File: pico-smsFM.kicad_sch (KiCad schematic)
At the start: 30 parts, among them J1 AudioJack3_SwitchTR, U1 Pico, U2 YM2413, U3 SN76489, U4 AE-Si5351A, U5 NJM4580, U6 4066

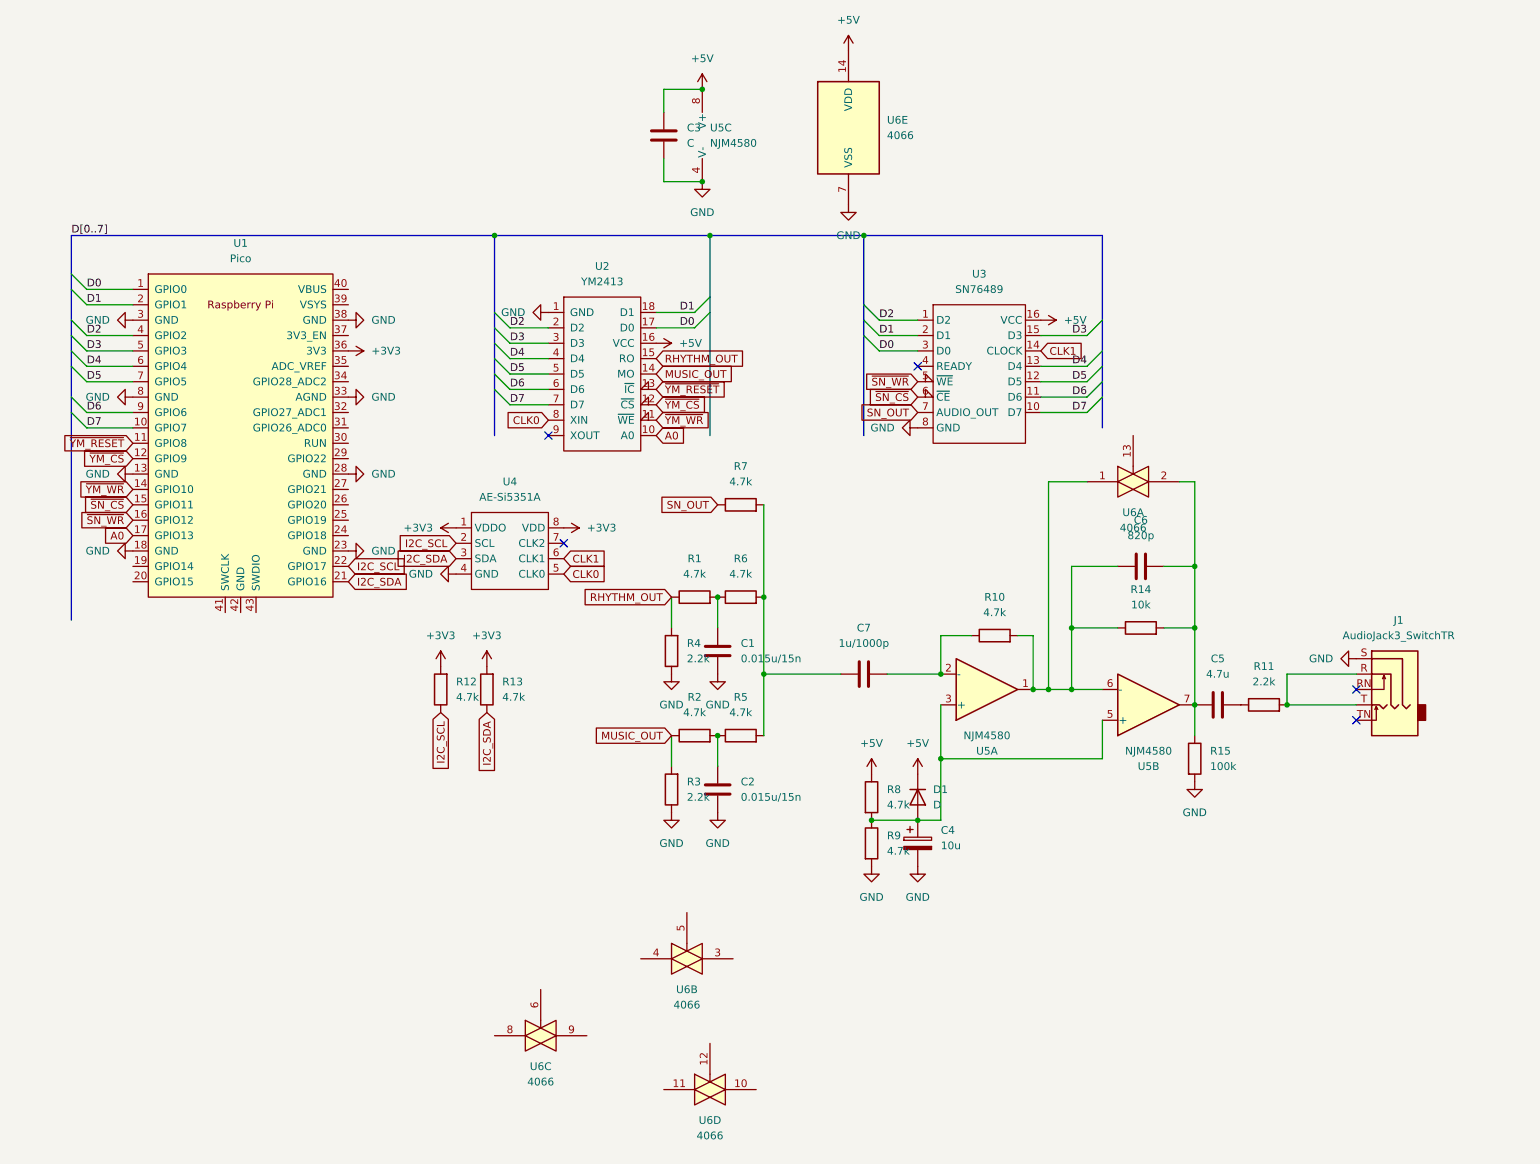
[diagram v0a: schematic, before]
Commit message: Add decoupling cap
Add more logic wire
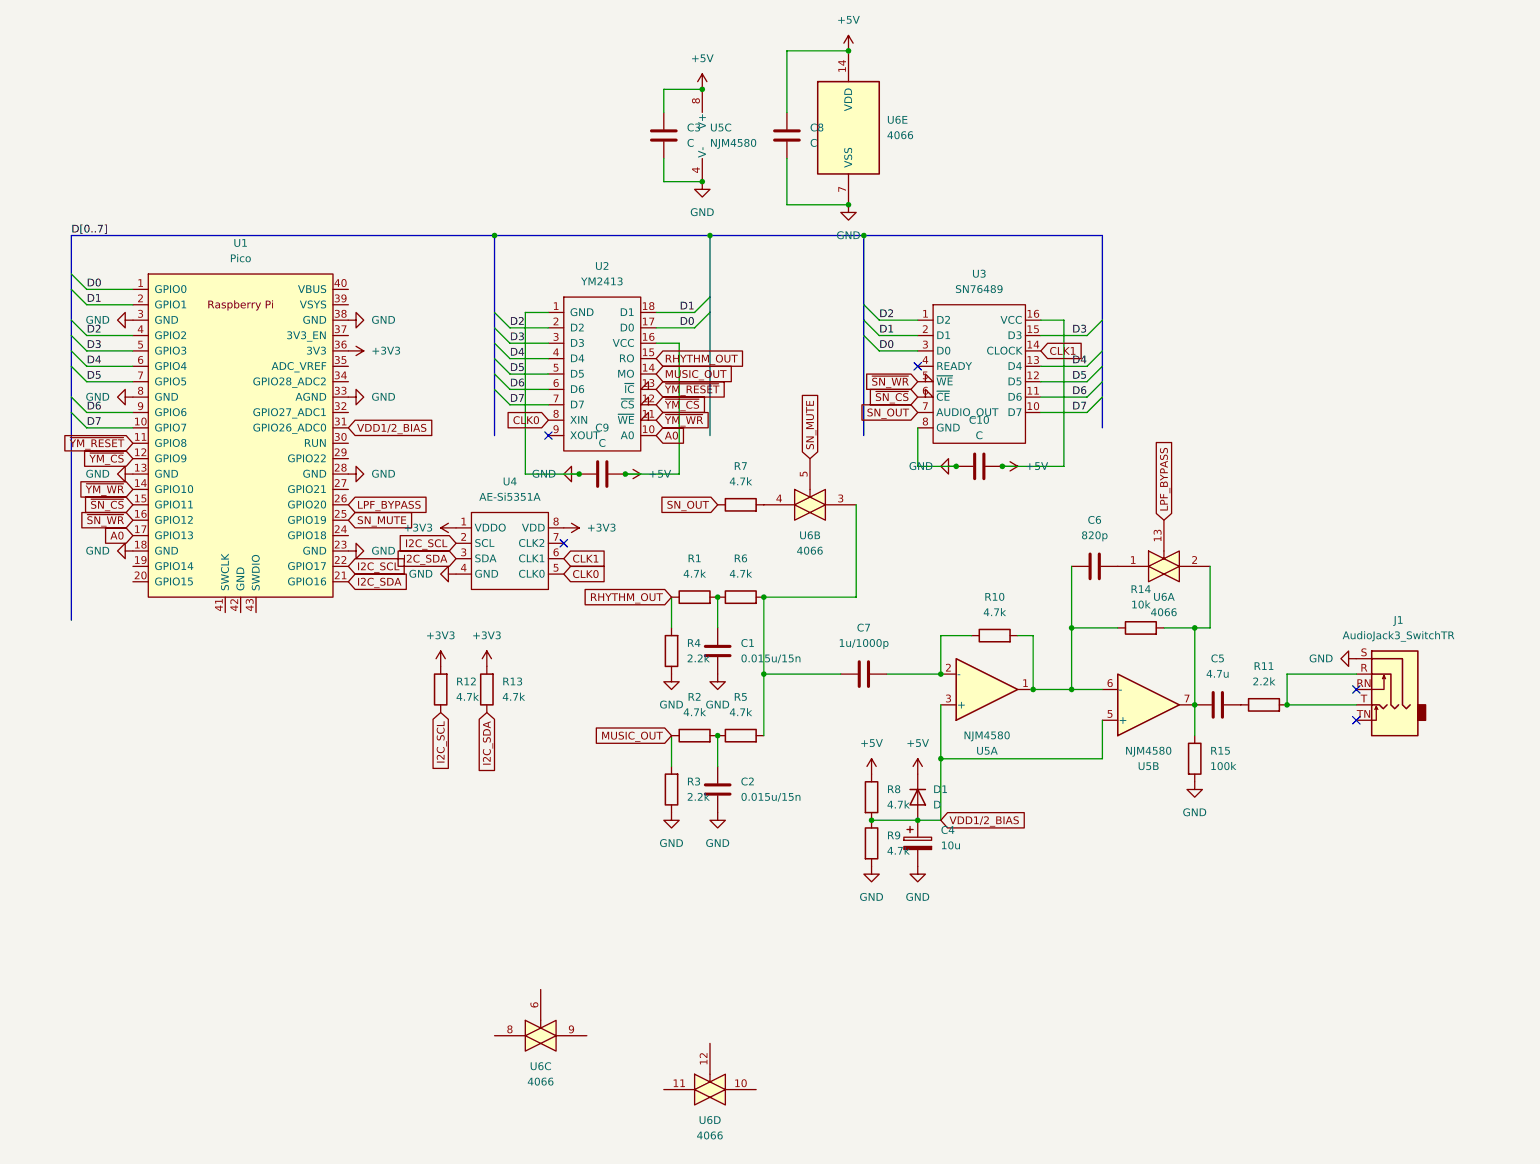
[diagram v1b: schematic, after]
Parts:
- added C10, C8, C9: C, Capacitor_THT:CP_Radial_D6.3mm_P2.50mm, symbol Device:C
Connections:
- net +5V: now also C10.2, C8.1, C9.2
- net GND: now also C10.1, C8.2, C9.1
- net VDD1/2_BIAS: now reaches C4.1, D1.2 (A), R8.2, R9.1, U5.3 (+), U5.5 (+)
- net VDD1/2_BIAS: now also U1.31 (GPIO26_ADC0)
- net at C7.1, R5.2, R6.2: now also U6.3; no longer R7.2
- net at C6.1, R10.2, R14.1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: no longer U6.1
- net at C5.1, R14.2, R15.1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: no longer C6.2
- net SN_MUTE: now reaches U1.25 (GPIO19)
- net SN_MUTE: now also U6.5
- net LPF_BYPASS: now reaches U1.26 (GPIO20)
- net LPF_BYPASS: now also U6.13
- net at U6.4: now also R7.2
- new net: C6.2, U6.1
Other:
- moved on the sheet: C6, U6B

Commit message: Add more logics
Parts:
- added 10kA (x3): R_Potentiometer, symbol Device:R_Potentiometer
- added C11, C12: C, symbol Device:C
- added D2, D3, D4, D5: WS2812B, LED_SMD:LED_WS2812B_PLCC4_5.0x5.0mm_P3.2mm, symbol LED:WS2812B
- added J2: Micro_SD_Card_Det2, symbol Connector:Micro_SD_Card_Det2
- added RN1: R_Network06, Resistor_THT:R_Array_SIP7, symbol Device:R_Network06
- added U7: MCP23017_SP, Package_DIP:DIP-28_W7.62mm, symbol Interface_Expansion:MCP23017_SP
- C10, C9: value C -> 0.1u/ceramic
- C3, C8: value C -> 0.1u
- R15: footprint (none) -> Resistor_THT:R_Axial_DIN0207_L6.3mm_D2.5mm_P10.16mm_Horizontal
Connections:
- net +3V3: now also C11.1, C12.1, D2.1 (VDD), D3.1 (VDD), D4.1 (VDD), D5.1 (VDD), J2.4 (VDD), RN1.1 (common)
- net GND: now also 10kA.3, 10kA.3, 10kA.3, C11.2, C12.2, D2.3 (VSS), D3.3 (VSS), D4.3 (VSS), D5.3 (VSS), J2.6 (VSS)
- net LPF_BYPASS: now also U7.22 (GPA1); no longer U1.26 (GPIO20)
- net SN_MUTE: now also U7.21 (GPA0); no longer U1.25 (GPIO19)
- net VDD1/2_BIAS: now also U1.32 (GPIO27_ADC1); no longer U1.31 (GPIO26_ADC0)
- net at C7.1, U6.3: now also 10kA.2, 10kA.2; no longer R5.2, R6.2
- net WS2812_DIN: now reaches U1.19 (GPIO14)
- net WS2812_DIN: now also D2.4 (DIN)
- net SDIO_DAT0: now reaches U1.24 (GPIO18)
- net SDIO_DAT0: now also J2.7 (DAT0), RN1.6 (R5)
- net SDIO_DAT3: now reaches U1.27 (GPIO21)
- net SDIO_DAT3: now also J2.2 (DAT3/CD), RN1.4 (R3)
- net SDIO_CMD: now reaches U1.29 (GPIO22)
- net SDIO_CMD: now also J2.3 (CMD), RN1.5 (R4)
- net at R7.2: now also 10kA.1; no longer U6.4
- new net: 10kA.2, U6.4
- new net: 10kA.1, R6.2
- new net: D4.2 (DOUT), D5.4 (DIN)
- new net: D3.2 (DOUT), D4.4 (DIN)
- new net: 10kA.1, R5.2
- new net: D2.2 (DOUT), D3.4 (DIN)
- new net SDIO_CLK: J2.5 (CLK), U1.31 (GPIO26_ADC0)
- new net SDIO_DAT1: J2.8 (DAT1), RN1.7 (R6), U1.25 (GPIO19)
- new net SDIO_DAT2: J2.1 (DAT2), RN1.3 (R2), U1.26 (GPIO20)
- no-connect marks 5 -> 10
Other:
- moved on the sheet: C1, C2, R1, R2, R3, R4, R5, R6, R7, U6B, U6C, U6D
